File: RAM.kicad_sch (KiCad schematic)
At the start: 8 parts, among them U2 TXB0108DQSR, U3 TXB0108DQSR, U4 TXB0108DQSR, U5 74LVC1G04, U6 TXB0108DQSR, U7 AS6C1616, U8 TXB0104D

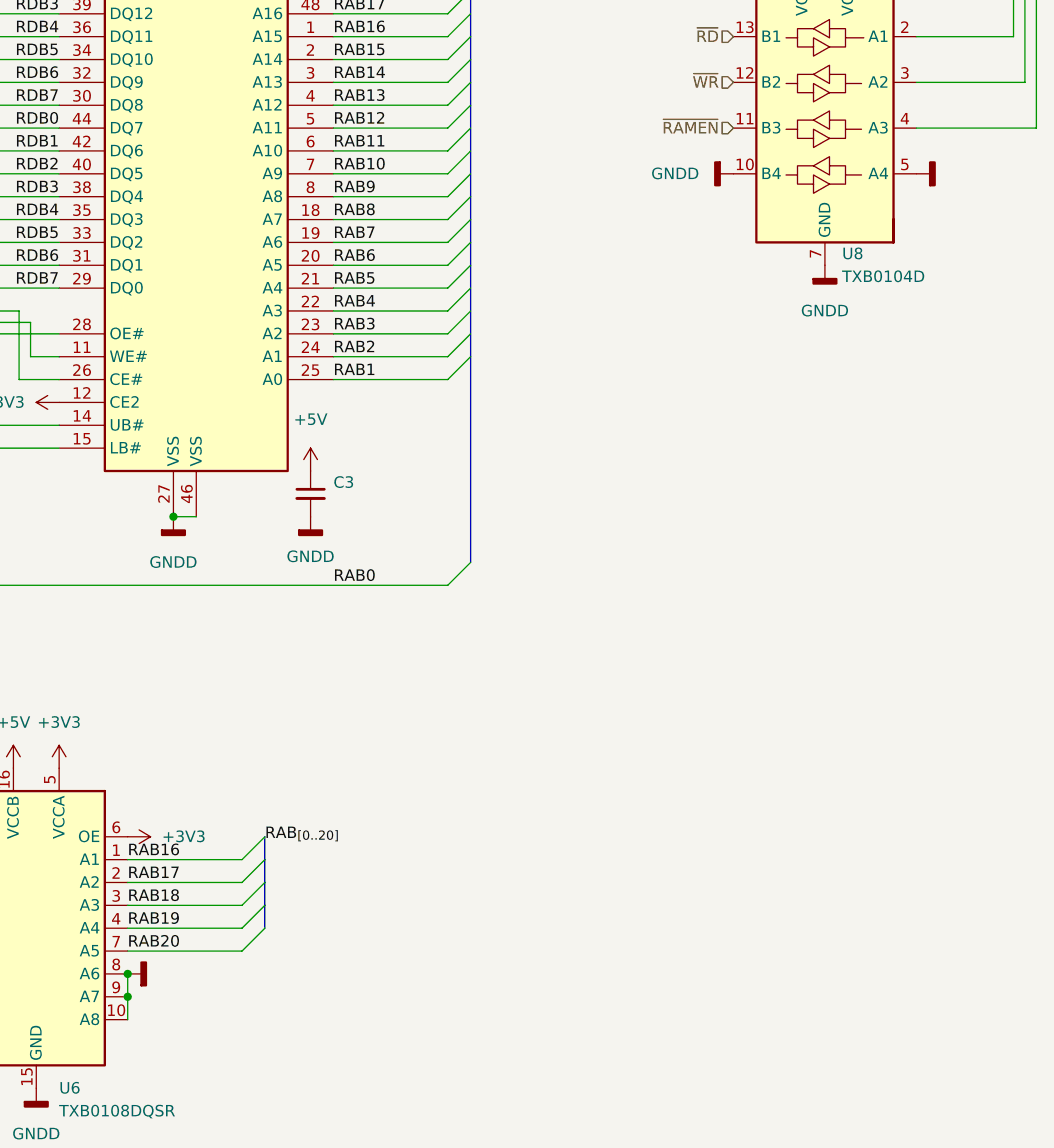
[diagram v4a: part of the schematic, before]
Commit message: begin integration of logic into atf1508
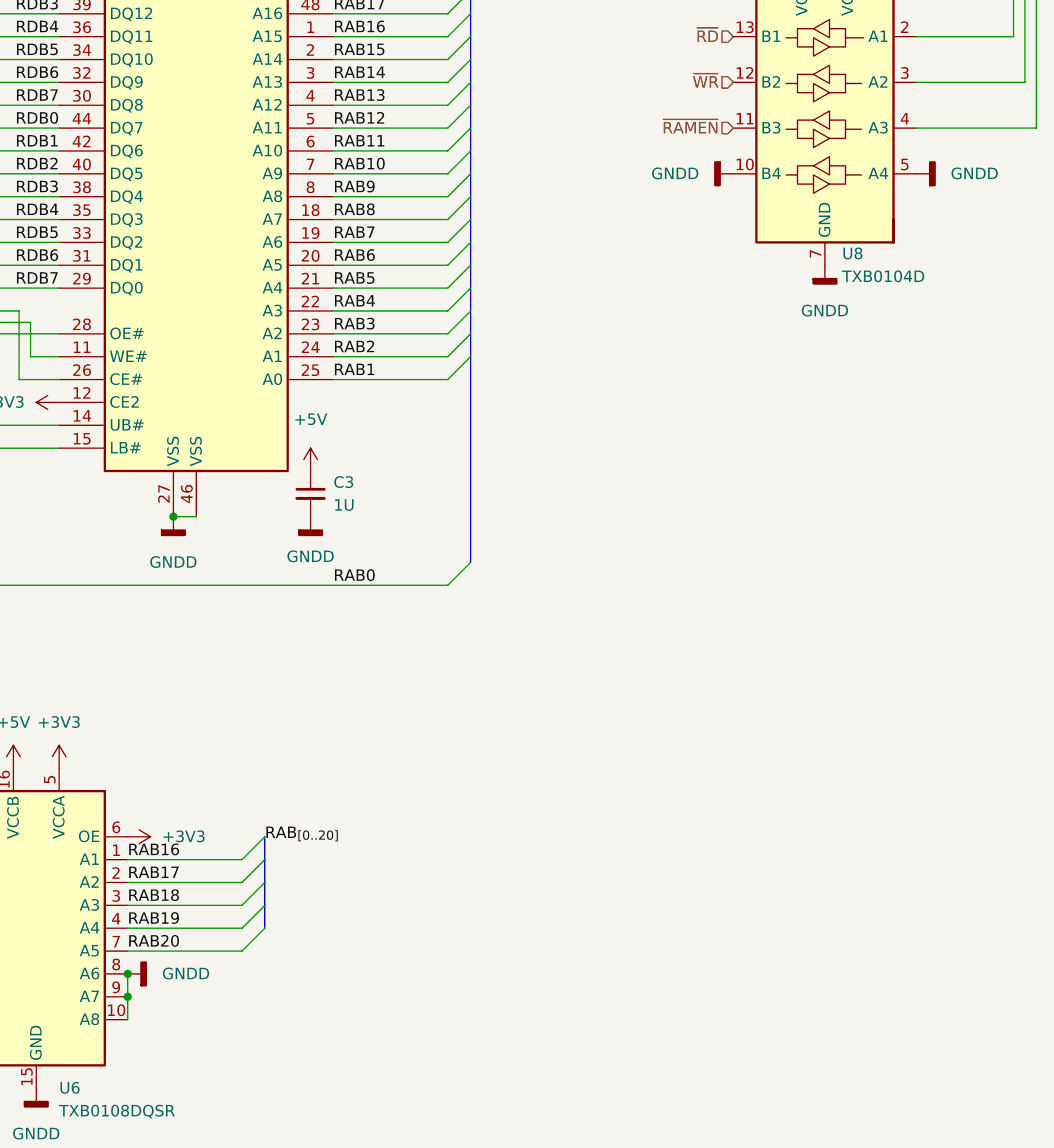
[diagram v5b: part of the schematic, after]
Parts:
- C3: value (none) -> 1U; footprint (none) -> Capacitor_SMD:C_1206_3216Metric
- U5: footprint (none) -> Package_TO_SOT_SMD:SOT-353_SC-70-5
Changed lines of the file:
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@@
     (property "Reference" "U5" (id 0) (at 100.33 85.09 0))
     (property "Value" "74LVC1G04" (id 1) (at 100.33 87.63 0))
-    (property "Footprint" "" (id 2) (at 107.95 91.44 0)
+    (property "Footprint" "Package_TO_SOT_SMD:SOT-353_SC-70-5" (id 2) (at 107.95 91.44 0)
       (effects (font (size 1.27 1.27)) hide)
     )
@@
       (effects (font (size 1.27 1.27)) hide)
     )
-    (property "Value" "" (id 1) (at 138.43 152.3999 90)
+    (property "Value" "GNDD" (id 1) (at 138.43 152.3999 90)
       (effects (font (size 1.27 1.27)) (justify right))
     )
@@
       (effects (font (size 1.27 1.27)) hide)
     )
-    (property "Value" "" (id 1) (at 226.06 63.4999 90)
+    (property "Value" "GNDD" (id 1) (at 226.06 63.4999 90)
       (effects (font (size 1.27 1.27)) (justify right))
     )
@@
       (effects (font (size 1.27 1.27)) (justify left))
     )
-    (property "Value" "" (id 1) (at 157.48 100.3362 0)
-      (effects (font (size 1.27 1.27)) (justify left))
-    )
-    (property "Footprint" "" (id 2) (at 154.94 99.06 0)
-      (effects (font (size 1.27 1.27)) hide)
-    )
+    (property "Value" "1U" (id 1) (at 157.48 100.3362 0)
+      (effects (font (size 1.27 1.27)) (justify left))
+    )
+    (property "Footprint" "Capacitor_SMD:C_1206_3216Metric" (id 2) (at 154.94 99.06 0)
+      (effects (font (size 1.27 1.27)) hide)
+    )

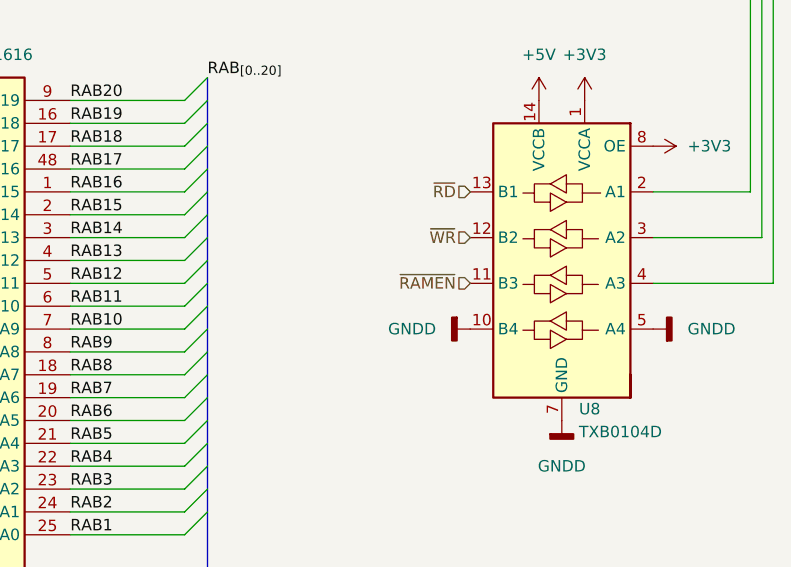
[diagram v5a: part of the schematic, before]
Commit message: added ATF150x part (specifically the 1508) vhdl file contains the (hopeful) implementition of the mapper
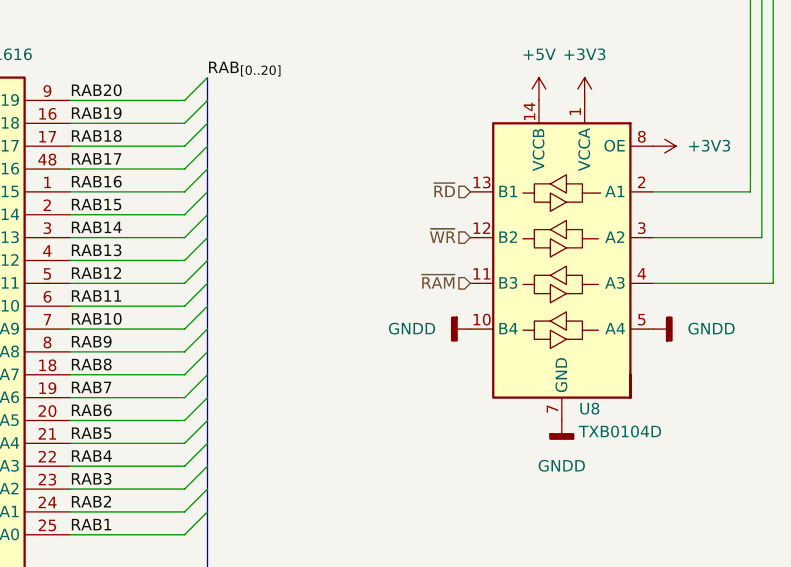
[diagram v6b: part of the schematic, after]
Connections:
- net ~{RAMEN} renamed ~{RAM}
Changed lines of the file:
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@@
     (effects (font (size 1.27 1.27)) (justify right))
   )
-  (hierarchical_label "~{RAMEN}" (shape input) (at 201.93 58.42 180)
+  (hierarchical_label "~{RAM}" (shape input) (at 201.93 58.42 180)
     (effects (font (size 1.27 1.27)) (justify right))
   )

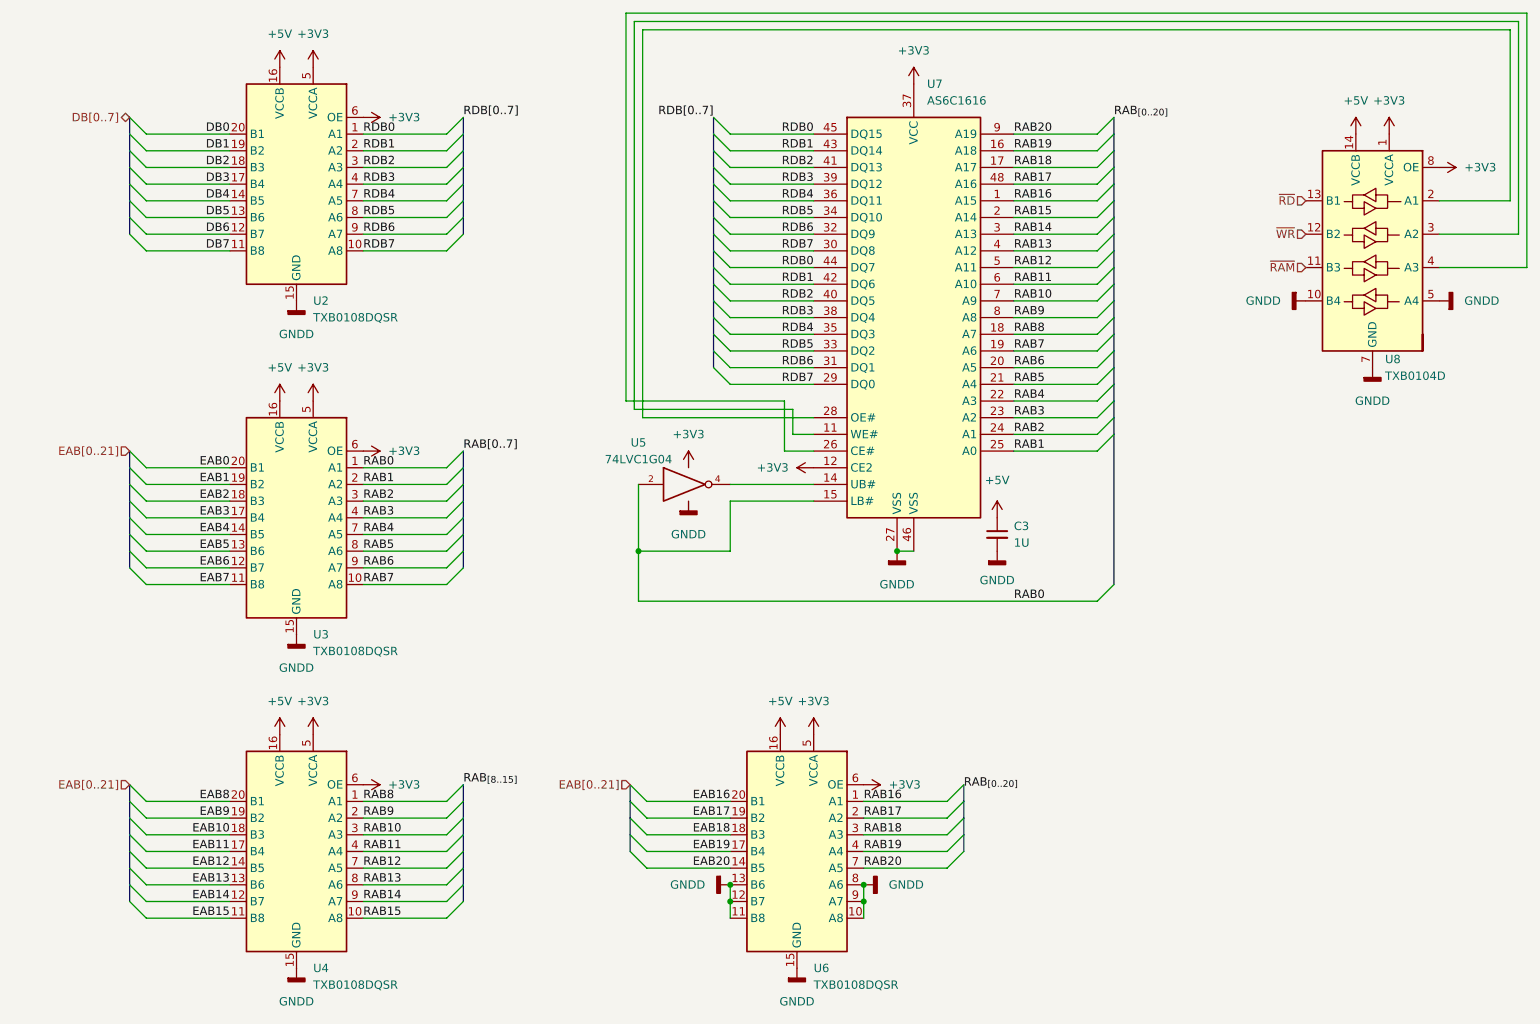
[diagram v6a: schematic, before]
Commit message: updated 84c10 pinout, apparently never checked for validity.... further simplification of dma and timer system (removed mode 2 interrupt structure, and interrupts in general) cleaned up vhdl code for 1508, still need testing to ensure functionality and that it even fits in the 1508....
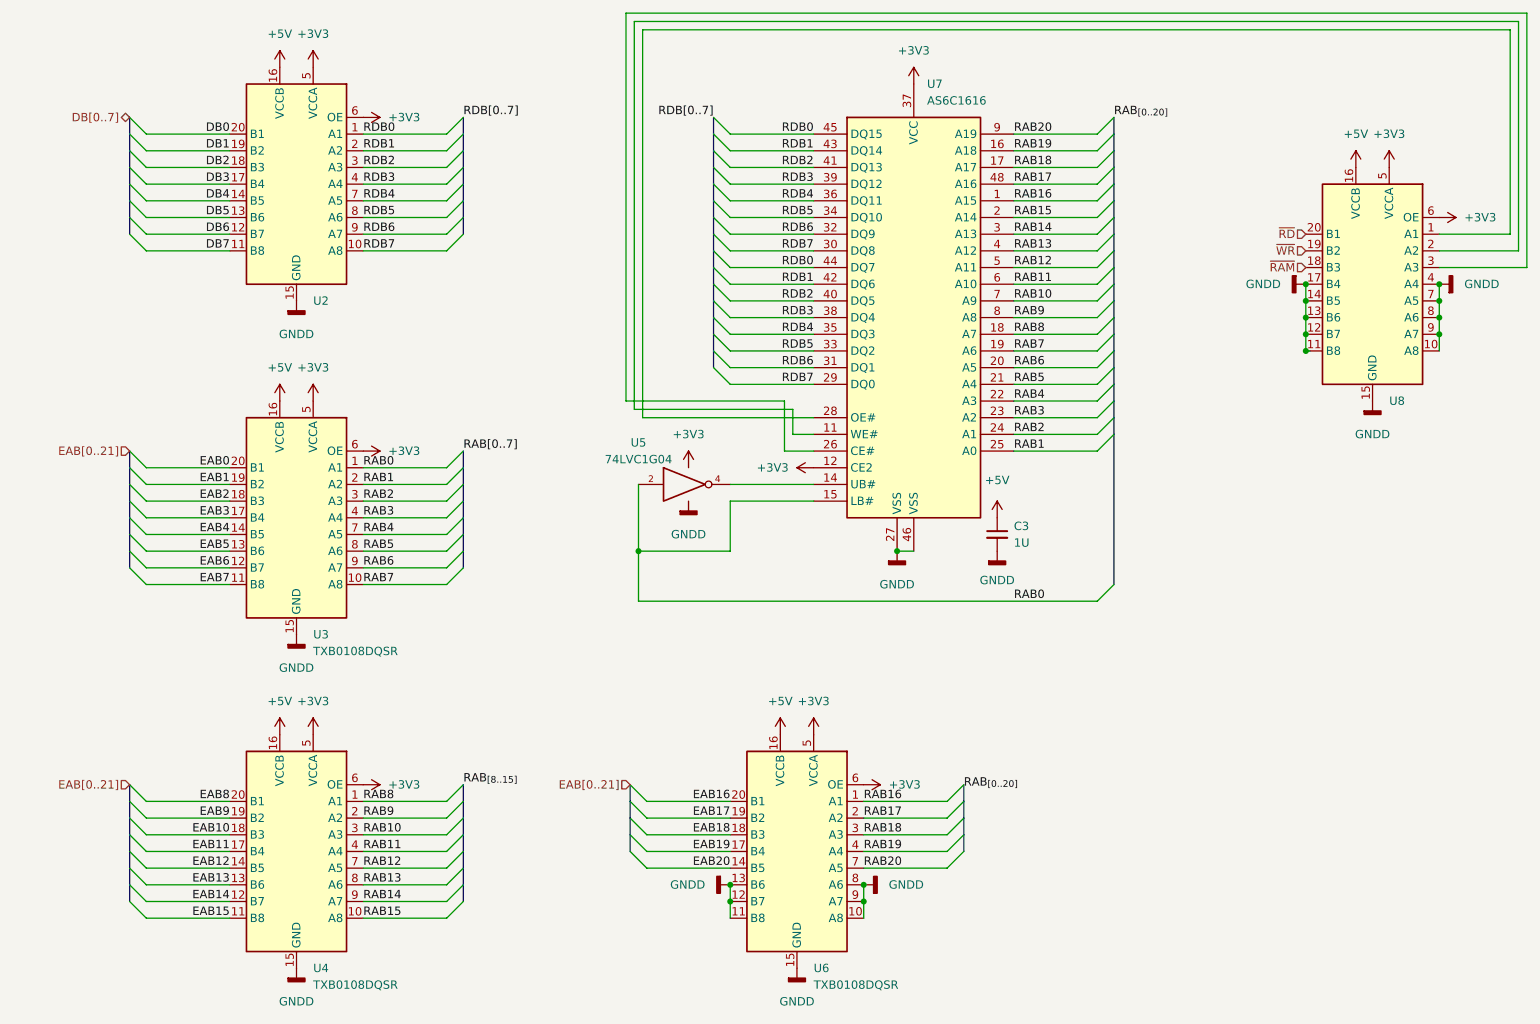
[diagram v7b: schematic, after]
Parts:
- removed U8: TXB0104D, Package_SO:SOIC-14_3.9x8.7mm_P1.27mm, symbol Logic_LevelTranslator:TXB0104D
- added U8: (no value), symbol Logic_LevelTranslator:TXB0108DQSR
- U2: value TXB0108DQSR -> (none); footprint Package_SON:USON-20_2x4mm_P0.4mm -> (none)
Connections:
- net +3V3: now also U8.5 (VCCA), U8.6 (OE)
- net +5V: now also U8.16 (VCCB)
- net GND: now also U8.10 (A8), U8.11 (B8), U8.12 (B7), U8.13 (B6), U8.14 (B5), U8.15 (GND), U8.17 (B4), U8.4 (A4), U8.7 (A5), U8.8 (A6), U8.9 (A7)
- net ~{RAM}: now also U8.18 (B3)
- net ~{RD}: now also U8.20 (B1)
- net ~{WR}: now also U8.19 (B2)
- net at U7.11 (WE#): now also U8.2 (A2)
- net at U7.26 (CE#): now also U8.3 (A3)
- net at U7.28 (OE#): now also U8.1 (A1)

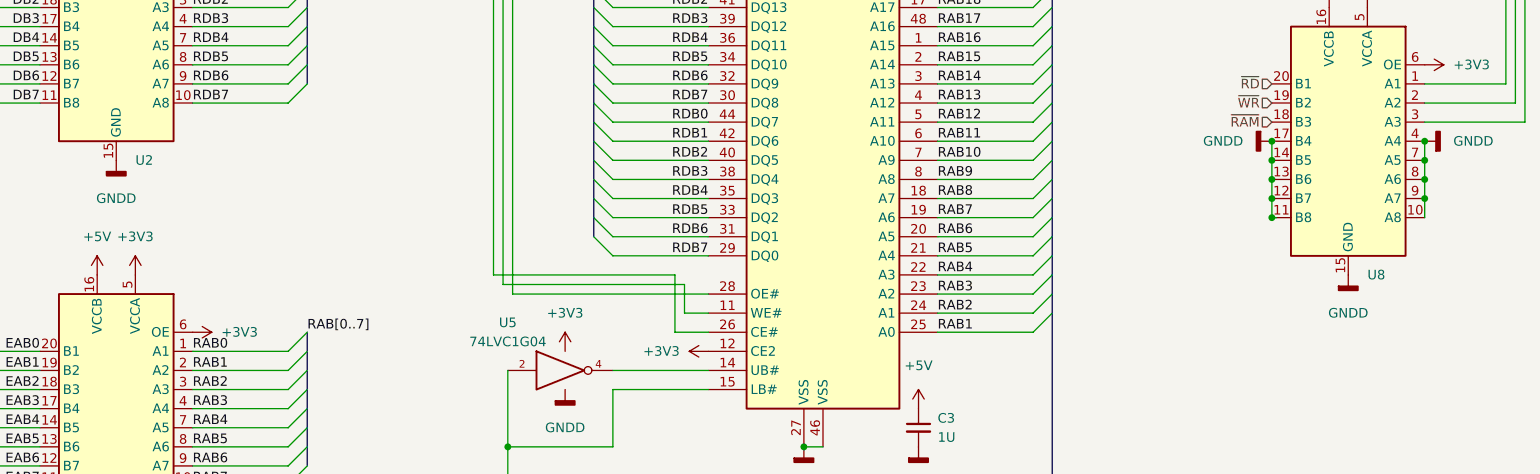
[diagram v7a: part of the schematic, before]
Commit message: forgot to actually add the previous fixes to kicad
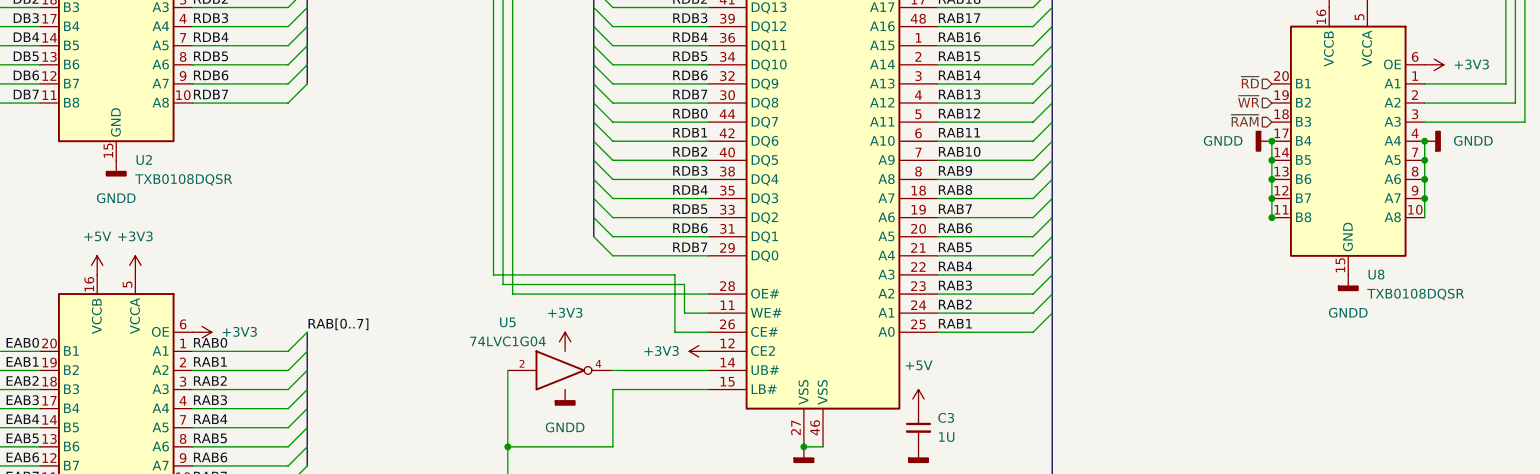
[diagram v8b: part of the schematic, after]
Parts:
- U2, U8: value (none) -> TXB0108DQSR; footprint (none) -> Package_SON:USON-20_2x4mm_P0.4mm
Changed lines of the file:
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@@
       (effects (font (size 1.27 1.27)) (justify right))
     )
-    (property "Value" "" (id 1) (at 50.8 66.04 0)
+    (property "Value" "TXB0108DQSR" (id 1) (at 50.8 66.04 0)
       (effects (font (size 1.27 1.27)) (justify right))
     )
-    (property "Footprint" "" (id 2) (at 48.26 64.77 0)
+    (property "Footprint" "Package_SON:USON-20_2x4mm_P0.4mm" (id 2) (at 48.26 64.77 0)
       (effects (font (size 1.27 1.27)) hide)
     )
@@
       (effects (font (size 1.27 1.27)) (justify right))
     )
-    (property "Value" "" (id 1) (at 214.63 81.28 0)
+    (property "Value" "TXB0108DQSR" (id 1) (at 214.63 81.28 0)
       (effects (font (size 1.27 1.27)) (justify right))
     )
-    (property "Footprint" "" (id 2) (at 212.09 80.01 0)
+    (property "Footprint" "Package_SON:USON-20_2x4mm_P0.4mm" (id 2) (at 212.09 80.01 0)
       (effects (font (size 1.27 1.27)) hide)
     )
